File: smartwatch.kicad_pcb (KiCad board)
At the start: 2 copper layers, 34.4 x 215.2 mm, 104 parts, among them J1 505148-0408, J2 505147-0490, J3 505110-2491, J4 503480-0600, Q1 Si1308EDL, Q2 Si1308EDL, Q3 Si1308EDL, SW1 SKTDLDE010, SW2 SKTDLDE010, SW3 SKTDLDE010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

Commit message: J3 and J4 SMD mounting pads are connected to +3V3 plane for stability. X2 is rotated to be alongside the bend radious if watch is worn. also for stability. traces leading to  buzzer are thickened for more current capacity.
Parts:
- moved L3 0.10 mm to (83.5, 125.9)
- moved X2 0.10 mm to (90.0, 129.7), turned to 270 degrees
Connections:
- J3 pad 25: (no net) -> +3V3
- J3 pad 26: (no net) -> +3V3
- J4 pad 7: (no net) -> +3V3
- J4 pad 8: (no net) -> +3V3
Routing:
- net Net-(L3-Pad2): track 9.37 -> 14.4 mm
- net -BATT: track 269.5 -> 266.7 mm, vias 67 -> 68
- net /SWDCLK: track 144.1 -> 144.9 mm
- net +3V3: track 42.5 -> 41.9 mm

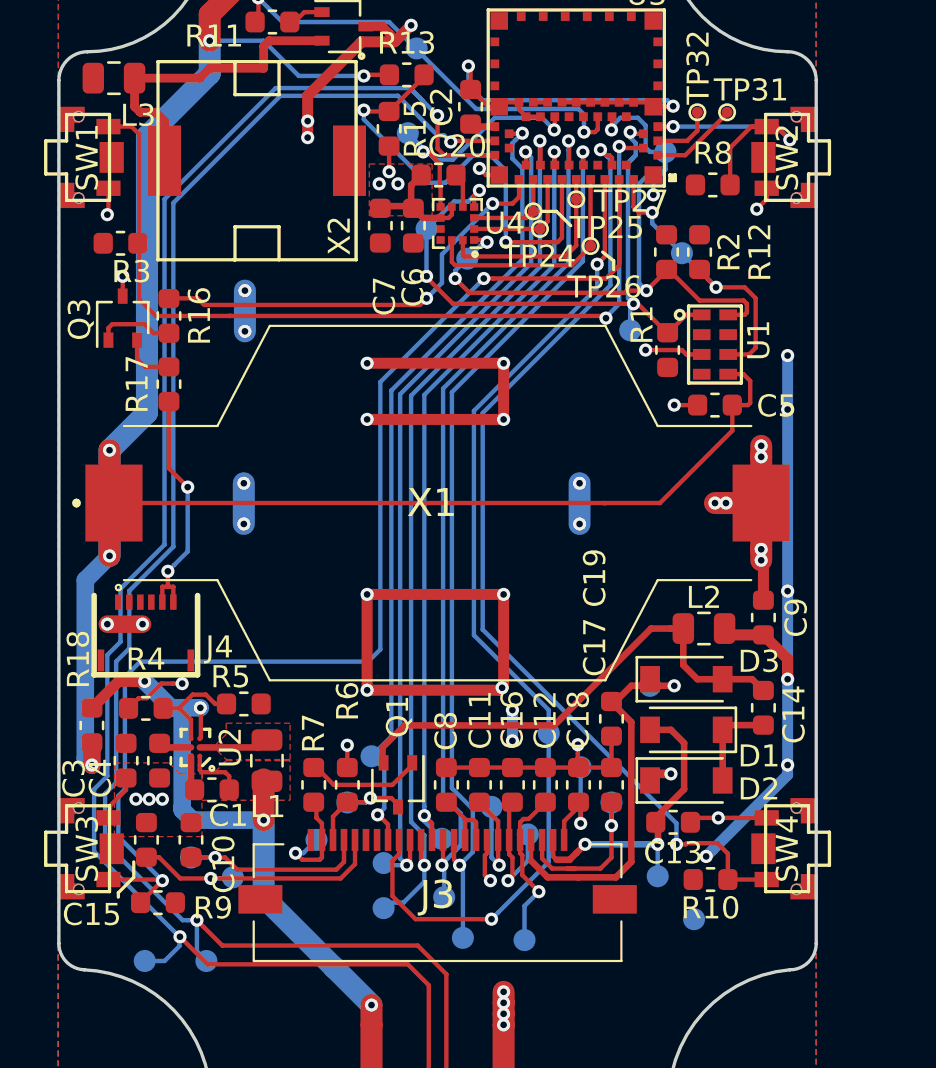
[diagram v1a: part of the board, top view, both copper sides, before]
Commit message: connect solder tabs of clasp connector J2 to plane for stability. pads are connected with thermal relief for easy soldering
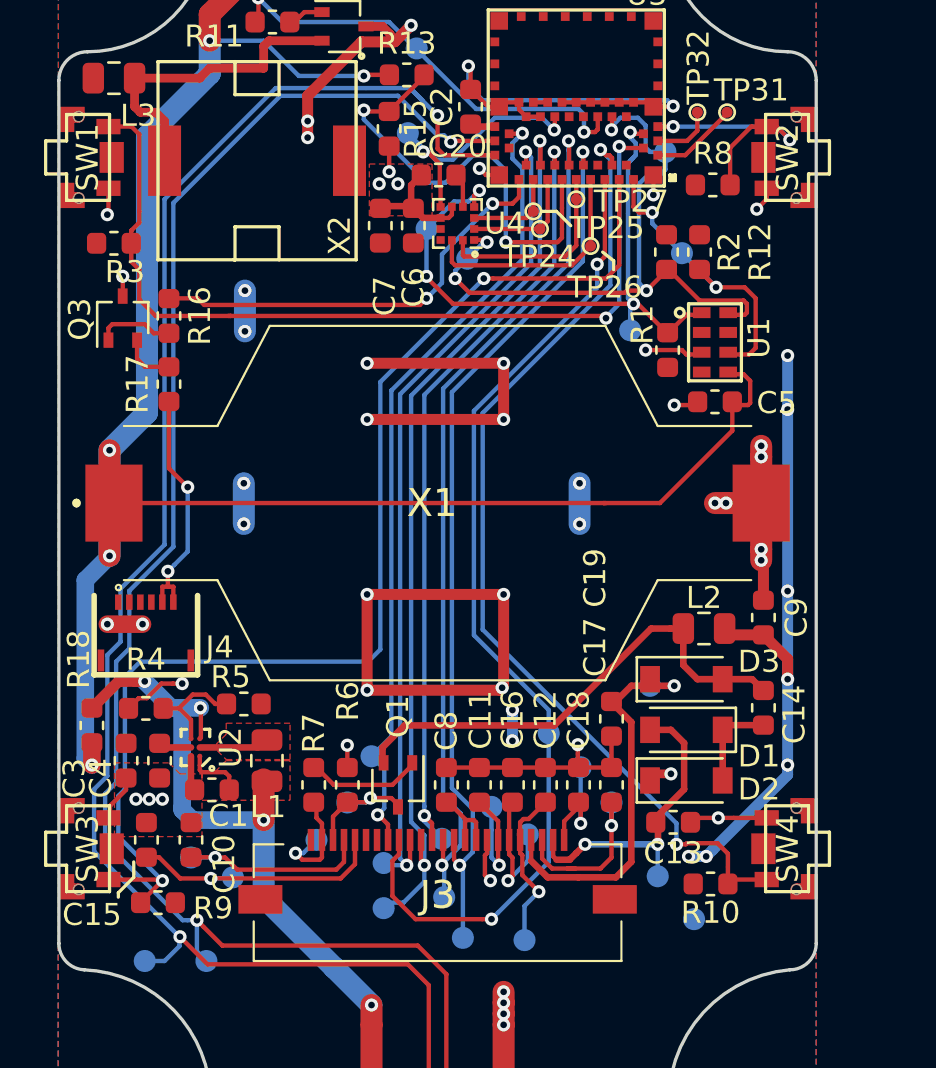
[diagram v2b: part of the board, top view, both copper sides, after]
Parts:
- moved R3 0.30 mm to (83.5, 133.4)
- moved R10 0.20 mm to (110.6, 162.5)
- moved C5 0.15 mm to (110.8, 140.6)
- moved U1 0.10 mm to (109.6, 136.2)
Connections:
- J2 pad ~: (no net) -> +3V3 (x11)
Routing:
- net +3V3: track 41.9 -> 42.7 mm, vias 14 -> 15

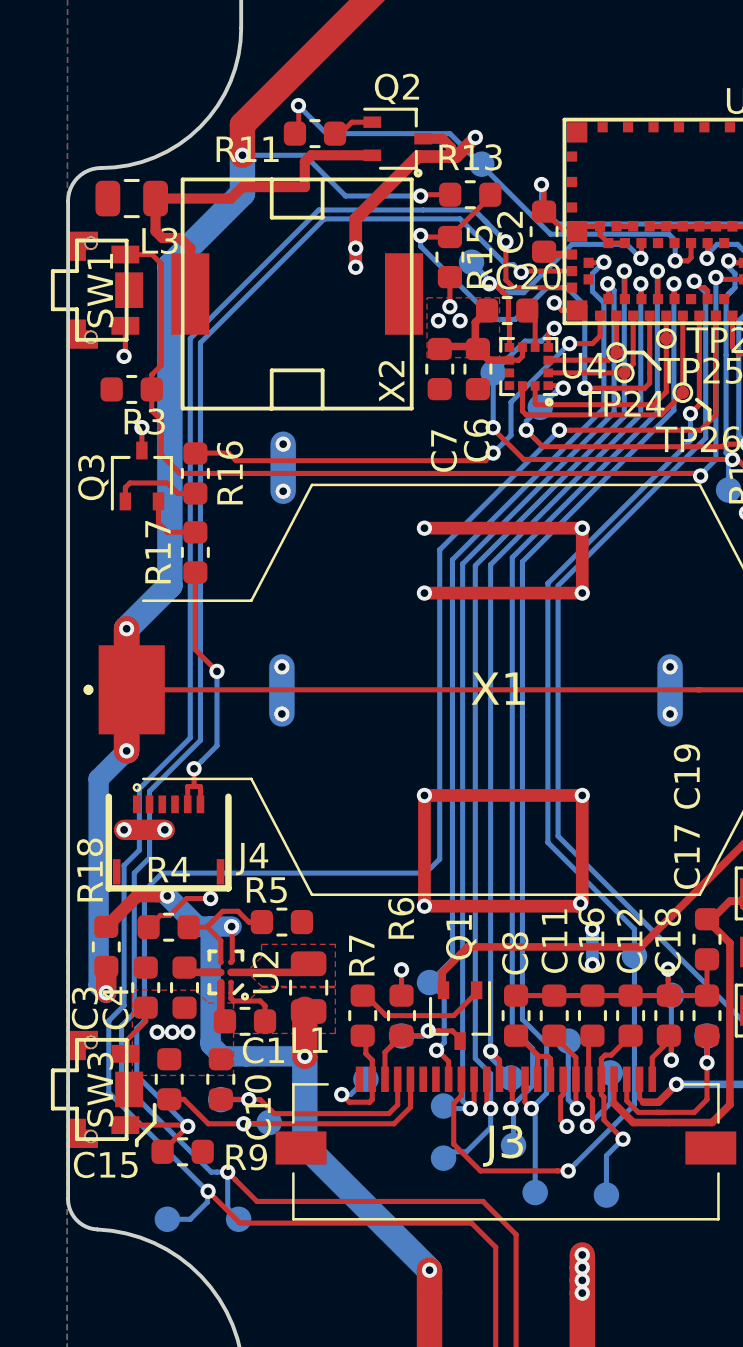
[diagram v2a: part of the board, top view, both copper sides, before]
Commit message: Fix: put L1 closer to SW pin of TPS610994; add more vias to power traces
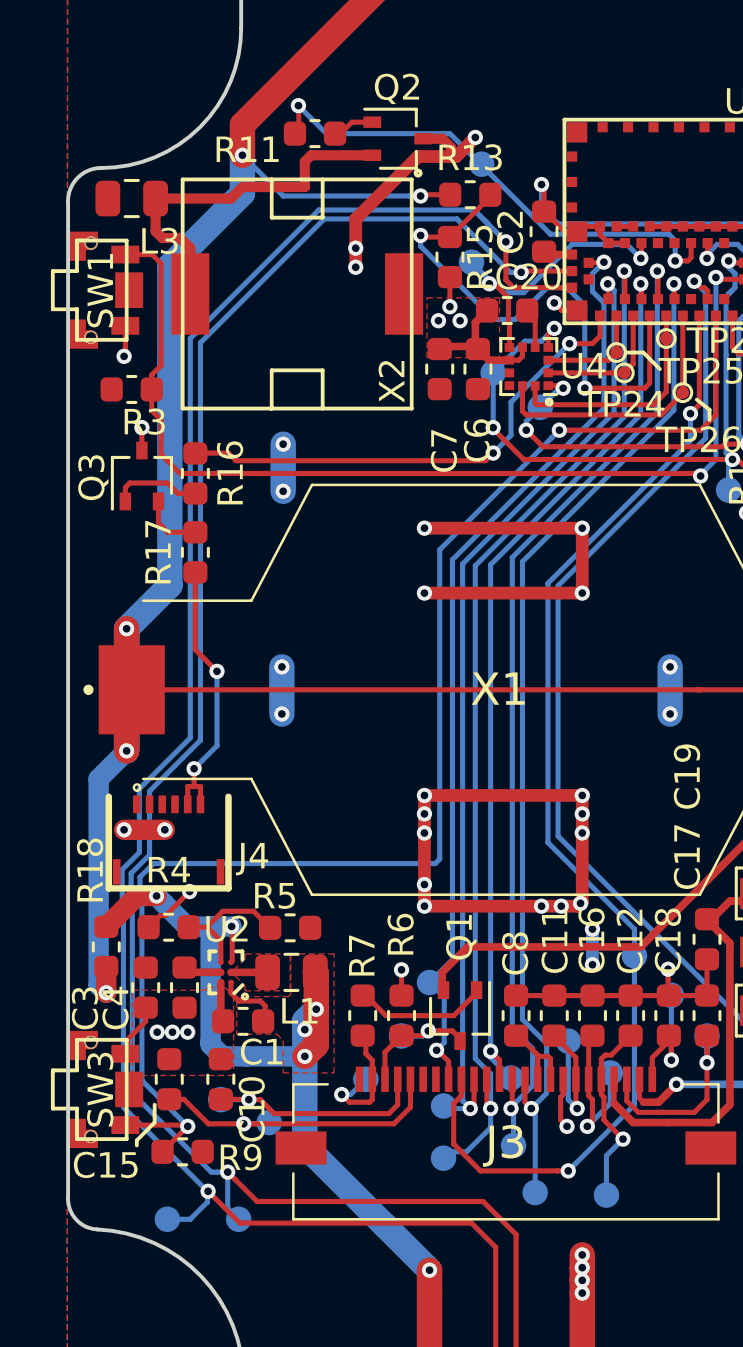
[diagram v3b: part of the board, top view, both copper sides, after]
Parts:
- moved L1 0.90 mm to (89.8, 156.3), turned to 180 degrees
- moved R5 0.40 mm to (89.7, 154.6)
- moved C1 0.08 mm to (87.9, 158.2)
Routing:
- net +VDC: track 105.1 -> 108.6 mm, vias 7 -> 9
- net Net-(L1-Pad2): track 3.00 -> 1.44 mm
- net -BATT: track 266.7 -> 265.9 mm, vias 68 -> 75

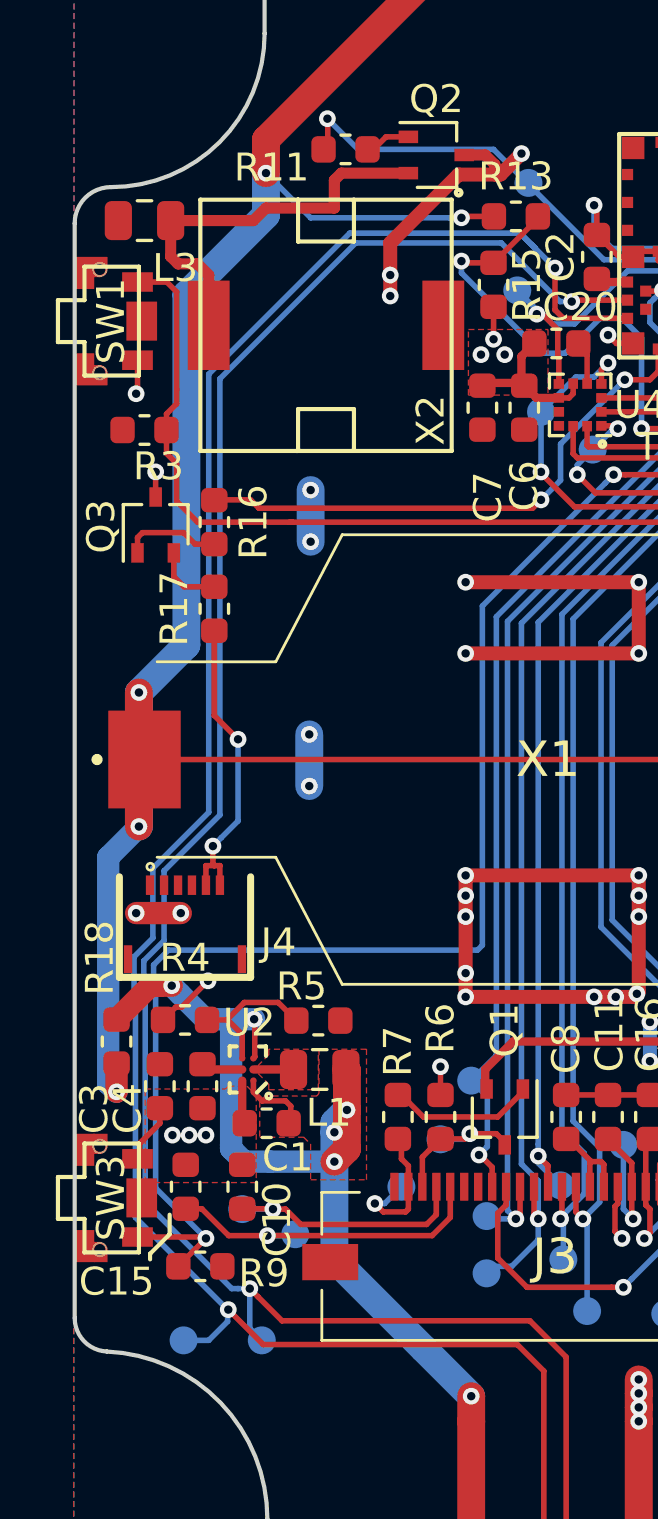
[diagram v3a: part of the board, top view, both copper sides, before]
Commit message: Fix: move via to close 3V3 plane next to batt+ voltage line.
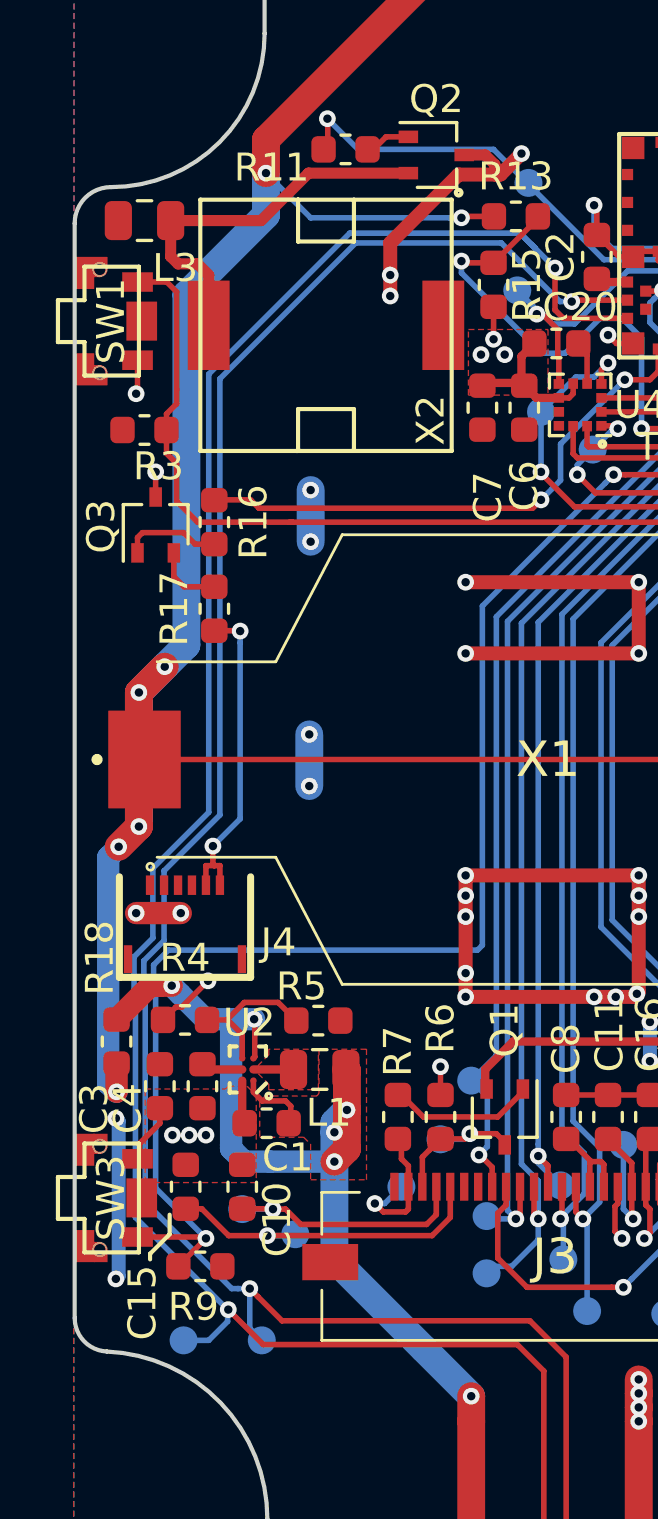
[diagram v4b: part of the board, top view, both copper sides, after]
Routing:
- net +3V3: track 42.7 -> 48.5 mm, vias 15 -> 17
- net +BATT: track 178.7 -> 181.1 mm, vias 5 -> 7
- net Net-(J4-Pad5): track 11.1 -> 11.7 mm
- net Net-(L3-Pad2): track 14.4 -> 13.8 mm
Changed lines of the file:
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@@
     (thickness 1.6)
     (drawings 166)
-    (tracks 970)
+    (tracks 978)
     (zones 0)
     (modules 104)
@@
   )
   (setup
-    (last_trace_width 1)
+    (last_trace_width 0.3)
     (user_trace_width 0.2)
     (user_trace_width 0.3)
@@
     (tags capacitor)
     (attr smd)
-    (fp_text reference C15 (at -3.4 -2.475) (layer F.SilkS)
+    (fp_text reference C15 (at -4.15 -1.55 90) (layer F.SilkS)
       (effects (font (size 1 1) (thickness 0.15)))
     )
@@
     (tags resistor)
     (attr smd)
-    (fp_text reference R9 (at -2.275 -0.25 180) (layer F.SilkS)
+    (fp_text reference R9 (at 0.25 -1.45 180) (layer F.SilkS)
       (effects (font (size 1 1) (thickness 0.15)))
     )
@@
   (via (at 109.6 161.25) (size 0.6) (drill 0.3) (layers F.Cu B.Cu) (net 3))
   (segment (start 110.399994 161.25) (end 109.6 161.25) (width 0.5) (layer B.Cu) (net 3))
+  (via (at 82.475 158.05) (size 0.6) (drill 0.3) (layers F.Cu B.Cu) (net 3))
+  (via (at 82.475 163.8) (size 0.6) (drill 0.3) (layers F.Cu B.Cu) (net 3))
+  (segment (start 82.575 163.7) (end 82.475 163.8) (width 0.5) (layer B.Cu) (net 3))
+  (segment (start 82.475 158.05) (end 82.575 158.15) (width 0.5) (layer B.Cu) (net 3))
+  (segment (start 82.575 158.15) (end 82.575 163.7) (width 0.5) (layer B.Cu) (net 3))
   (segment (start 87 161.3875) (end 87.0375 161.3875) (width 0.2) (layer F.Cu) (net 4))
   (segment (start 93.95 161.5) (end 93.95 160.5) (width 0.2) (layer F.Cu) (net 4))
@@
   (segment (start 112.3 140.75) (end 111.5875 140.75) (width 0.2) (layer F.Cu) (net 18))
   (segment (start 112.4 140.65) (end 112.3 140.75) (width 0.2) (layer F.Cu) (net 18))
-  (segment (start 85 141.1) (end 83.3 142.8) (width 1) (layer B.Cu) (net 18))
   (segment (start 85 128.55) (end 85 141.1) (width 1) (layer B.Cu) (net 18))
   (segment (start 87.85 124.2) (end 87.85 123) (width 1) (layer F.Cu) (net 18))
@@
   (via (at 82.5 157.1) (size 0.6) (drill 0.3) (layers F.Cu B.Cu) (net 18))
   (segment (start 82.5 157.1) (end 82.5 156.0875) (width 0.8) (layer F.Cu) (net 18))
-  (segment (start 82.200001 156.800001) (end 82.5 157.1) (width 0.8) (layer B.Cu) (net 18))
-  (segment (start 83.3 147.6) (end 82.200001 148.699999) (width 0.8) (layer B.Cu) (net 18))
-  (segment (start 82.200001 148.699999) (end 82.200001 156.800001) (width 0.8) (layer B.Cu) (net 18))
   (segment (start 108.3 145.2) (end 105.75 145.2) (width 0.2) (layer F.Cu) (net 18))
   (segment (start 111.5875 140.75) (end 111.5875 141.9125) (width 0.2) (layer F.Cu) (net 18))
@@
   (segment (start 89.449979 125.799979) (end 94.425736 125.799979) (width 0.2) (layer B.Cu) (net 18))
   (segment (start 94.425736 125.799979) (end 94.85 125.799979) (width 0.2) (layer B.Cu) (net 18))
+  (via (at 84.225 141.875) (size 0.6) (drill 0.3) (layers F.Cu B.Cu) (net 18))
+  (segment (start 83.3 142.8) (end 84.225 141.875) (width 1) (layer F.Cu) (net 18))
+  (segment (start 85 141.1) (end 84.225 141.875) (width 1) (layer B.Cu) (net 18))
+  (segment (start 84.225 141.875) (end 83.3 142.8) (width 1) (layer B.Cu) (net 18))
+  (via (at 82.575001 148.324999) (size 0.6) (drill 0.3) (layers F.Cu B.Cu) (net 18))
+  (segment (start 82.5 157.1) (end 82.200001 156.800001) (width 0.8) (layer B.Cu) (net 18))
+  (segment (start 82.200001 156.800001) (end 82.200001 148.699999) (width 0.8) (layer B.Cu) (net 18))
+  (segment (start 83.3 147.6) (end 82.575001 148.324999) (width 0.8) (layer B.Cu) (net 18))
+  (segment (start 83.3 147.6) (end 82.575001 148.324999) (width 1) (layer F.Cu) (net 18))
+  (segment (start 82.200001 148.699999) (end 82.575001 148.324999) (width 0.8) (layer B.Cu) (net 18))
   (segment (start 87.4 156.3) (end 88.8375 156.3) (width 0.3) (layer F.Cu) (net 19))
   (segment (start 96.15 158) (end 97.15 157) (width 0.2) (layer F.Cu) (net 20))
@@
   (segment (start 96 123.35) (end 99.95 127.3) (width 0.2) (layer B.Cu) (net 70))
   (via (at 90.05 122.25) (size 0.6) (drill 0.3) (layers F.Cu B.Cu) (net 70))
-  (segment (start 90.3 124.45) (end 90.3 125.45) (width 0.4) (layer F.Cu) (net 71))
-  (segment (start 87.85 125.45) (end 87.4 125.9) (width 0.4) (layer F.Cu) (net 71))
-  (segment (start 87.4 125.9) (end 84.4375 125.9) (width 0.4) (layer F.Cu) (net 71))
-  (segment (start 87.85 125.45) (end 90.3 125.45) (width 0.4) (layer F.Cu) (net 71))
-  (segment (start 92.85 124.2) (end 90.55 124.2) (width 0.4) (layer F.Cu) (net 71))
-  (segment (start 90.55 124.2) (end 90.3 124.45) (width 0.4) (layer F.Cu) (net 71))
   (segment (start 85.8 127.85) (end 85.4 127.45) (width 0.4) (layer F.Cu) (net 71))
   (segment (start 84.7 127.45) (end 84.4375 127.1875) (width 0.4) (layer F.Cu) (net 71))
@@
   (segment (start 85.4 127.45) (end 84.7 127.45) (width 0.4) (layer F.Cu) (net 71))
   (segment (start 85.8 129.65) (end 85.8 127.85) (width 0.4) (layer F.Cu) (net 71))
+  (segment (start 87.675 125.9) (end 84.4375 125.9) (width 0.4) (layer F.Cu) (net 71))
+  (segment (start 92.85 124.2) (end 89.375 124.2) (width 0.4) (layer F.Cu) (net 71))
+  (segment (start 89.375 124.2) (end 87.675 125.9) (width 0.4) (layer F.Cu) (net 71))
   (segment (start 99.35 130.7125) (end 98.9375 130.3) (width 0.2) (layer F.Cu) (net 72))
   (segment (start 99.35 131.7375) (end 99.35 130.7125) (width 0.2) (layer F.Cu) (net 72))
@@
   (segment (start 84.55 137.8) (end 84.55 138.65) (width 0.2) (layer F.Cu) (net 76))
   (segment (start 84.55 138.65) (end 84.9125 139.0125) (width 0.2) (layer F.Cu) (net 76))
-  (via (at 86.85 144.475) (size 0.6) (drill 0.3) (layers F.Cu B.Cu) (net 77))
-  (segment (start 86 140.5875) (end 86 143.625) (width 0.2) (layer F.Cu) (net 77))
-  (segment (start 86 143.625) (end 86.85 144.475) (width 0.2) (layer F.Cu) (net 77))
   (segment (start 85.95 148.724262) (end 85.95 148.299998) (width 0.2) (layer F.Cu) (net 77))
-  (segment (start 86.85 147.399998) (end 86.249999 147.999999) (width 0.2) (layer B.Cu) (net 77))
   (segment (start 86 149) (end 85.95 148.95) (width 0.2) (layer F.Cu) (net 77))
   (via (at 85.95 148.299998) (size 0.6) (drill 0.3) (layers F.Cu B.Cu) (net 77))
-  (segment (start 86.85 144.475) (end 86.85 147.399998) (width 0.2) (layer B.Cu) (net 77))
   (segment (start 85.95 148.95) (end 85.95 148.724262) (width 0.2) (layer F.Cu) (net 77))
-  (segment (start 86.249999 147.999999) (end 85.95 148.299998) (width 0.2) (layer B.Cu) (net 77))
   (segment (start 85.7 149) (end 86 149) (width 0.2) (layer F.Cu) (net 77))
   (segment (start 85.7 149.7) (end 85.7 149) (width 0.2) (layer F.Cu) (net 77))
   (segment (start 86.2 149) (end 86.2 149.7) (width 0.2) (layer F.Cu) (net 77))
   (segment (start 86 149) (end 86.2 149) (width 0.2) (layer F.Cu) (net 77))
+  (via (at 86.925 140.6) (size 0.6) (drill 0.3) (layers F.Cu B.Cu) (net 77))
+  (segment (start 86 140.5875) (end 86.9125 140.5875) (width 0.2) (layer F.Cu) (net 77))
+  (segment (start 86.9125 140.5875) (end 86.925 140.6) (width 0.2) (layer F.Cu) (net 77))
+  (segment (start 85.95 148.299998) (end 86.925 147.324998) (width 0.2) (layer B.Cu) (net 77))
+  (segment (start 86.925 147.324998) (end 86.925 141.024264) (width 0.2) (layer B.Cu) (net 77))
+  (segment (start 86.925 141.024264) (end 86.925 140.6) (width 0.2) (layer B.Cu) (net 77))
   (segment (start 110 128.2843) (end 110 127.803553) (width 0.2) (layer F.Cu) (net 80))
   (segment (start 110 127.803553) (end 110 127.45) (width 0.2) (layer F.Cu) (net 80))
